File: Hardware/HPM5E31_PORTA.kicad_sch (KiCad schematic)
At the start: 5 parts, among them U1 HPM5E31IGN1

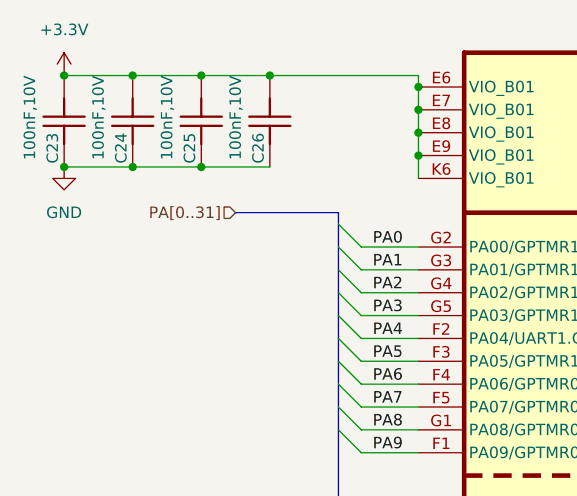
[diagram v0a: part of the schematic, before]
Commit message: 新增ESC IO引出，ESC CTR LED，EUI接口
编码器接口电源输出加保险，SPI加ESD
PY32ADC外部接口加ESD
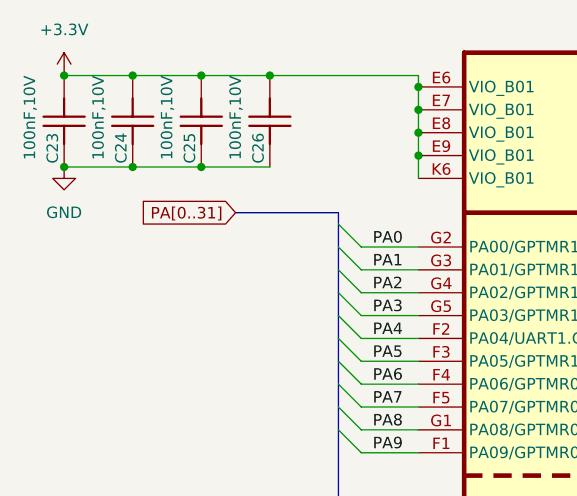
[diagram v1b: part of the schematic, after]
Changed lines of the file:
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@@
 		)
 	)
-	(hierarchical_label "PA[0..31]"
+	(global_label "PA[0..31]"
 		(shape input)
 		(at 99.06 64.77 180)
+		(fields_autoplaced yes)
 		(effects
 			(font
@@
 			(justify right)
 		)
+		(property "Intersheetrefs" "${INTERSHEET_REFS}"
+			(at 87.1847 64.77 0)
+			(effects
+				(font
+					(size 1.27 1.27)
+				)
+				(justify right)
+				(hide yes)
+			)
+		)
 	)

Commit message: 拉线
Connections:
- net +3.3V: now also U1.M1 (DCDC_IN), U1.M2 (DCDC_IN); no longer U1.E6 (VIO_B01), U1.E7 (VIO_B01), U1.E8 (VIO_B01), U1.E9 (VIO_B01), U1.K6 (VIO_B01)
- net PA0: no longer U1.G2 (PA00/GPTMR1.COMP0/UART0.TXD/MCAN0.TXD/PWM0.P0/TRGM.P00/SYSCTL.CLK_OBS0)
- net PA1: no longer U1.G3 (PA01/GPTMR1.CAPT0/UART0.RXD/MCAN0.RXD/PWM0.P1/TRGM.P01/SYSCTL.CLK_OBS2)
- net PA16: no longer U1.L1 (PA16/GPTMR3.COMP0/UART4.TXD/ESC0.P0_RXDV/QEO1.A/SDM0.DAT3/EUI0.CK)
- net PA17: now also U1.H8 (VSSA); no longer U1.L2 (PA17/GPTMR3.CAPT0/UART4.RXD/ESC0.P0_RXD0/QEO1.B/SDM0.CLK3/EUI0.SH)
- net PA18: no longer U1.K1 (PA18/GPTMR3.COMP1/UART4.DE/UART4.RTS/ESC0.P0_RXD1/QEO1.Z/SDM0.DAT2/EUI0.DI)
- net PA19: no longer U1.K2 (PA19/GPTMR3.CAPT1/UART4.CTS/SPI3.CS3/ESC0.P0_RXD2/SDM0.CLK2/EUI0.DO)
- net PA2: no longer U1.G4 (PA02/GPTMR1.COMP1/UART0.DE/UART0.RTS/I2C2.SCL/MCAN0.STBY/PWM0.P2/TRGM.P02/SYSCTL.CLK_OBS1)
- net PA20: no longer U1.J1 (PA20/UART5.CTS/SPI2.SCLK/ESC0.P0_RXD3/SDM0.DAT1)
- net PA21: no longer U1.J2 (PA21/GPTMR3.COMP2/UART5.DE/UART5.RTS/SPI2.CS0/ESC0.P0_RXCK/QEO0.Z/SDM0.CLK1/OWR0.DAT)
- net PA22: no longer U1.H1 (PA22/GPTMR2.CAPT0/UART5.RXD/SPI2.MISO/ETH0.TXER/QEO0.B/SDM0.DAT0/OWR1.DAT)
- net PA23: no longer U1.H2 (PA23/GPTMR2.COMP0/UART5.TXD/SPI2.MOSI/ESC0.P0_RXER/ETH0.RXER/QEO0.A/SDM0.CLK0)
- net PA24: no longer U1.K3 (PA24/GPTMR2.COMP1/UART6.TXD/SPI3.CS2/ESC0.P0_TXCK)
- net PA25: no longer U1.K4 (PA25/GPTMR2.CAPT1/UART6.RXD/SPI3.CS1/ESC0.P0_TXD0/ESC0.CTR0)
- net PA26: no longer U1.J3 (PA26/GPTMR2.COMP2/UART6.DE/UART6.RTS/SPI3.SCLK/ESC0.P0_TXD1/QEI1.H1/EWDG0.RST)
- net PA27: no longer U1.J4 (PA27/UART6.CTS/SPI3.CS0/ESC0.P0_TXD2/QEI1.F)
- net PA28: no longer U1.J5 (PA28/UART7.CTS/SPI3.MISO/ESC0.P0_TXD3/ESC0.CTR1/QEI1.H0)
- net PA29: no longer U1.H3 (PA29/GPTMR3.COMP3/UART7.DE/UART7.RTS/SPI3.MOSI/ESC0.P0_TXEN/QEI1.Z)
- net PA3: no longer U1.G5 (PA03/GPTMR1.CAPT1/UART0.CTS/I2C2.SDA/MCAN1.STBY/PWM0.P3/TRGM.P03/SYSCTL.CLK_OBS3)
- net PA30: no longer U1.H4 (PA30/UART7.RXD/SPI3.DAT2/ESC0.MDIO/ETH0.MDIO/QEI1.A)
- net PA31: no longer U1.H5 (PA31/GPTMR2.COMP3/UART7.TXD/SPI3.DAT3/ESC0.MDC/ETH0.MDC/QEI1.B)
- net PA4: no longer U1.F2 (PA04/UART1.CTS/SPI1.SCLK/MCAN1.RXD/PWM0.P4/TRGM.P04/JTAG.TDO)
- net PA5: no longer U1.F3 (PA05/GPTMR1.COMP2/UART1.DE/UART1.RTS/SPI1.CS0/MCAN1.TXD/PWM0.P5/TRGM.P05/JTAG.TDI)
- net PA6: no longer U1.F4 (PA06/GPTMR0.CAPT0/UART1.RXD/I2C3.SDA/SPI1.MISO/PWM0.P6/TRGM.P06/JTAG.TCK)
- net PA7: no longer U1.F5 (PA07/GPTMR0.COMP0/UART1.TXD/I2C3.SCL/SPI1.MOSI/PWM0.P7/TRGM.P07/JTAG.TMS)
- net PA8: no longer U1.G1 (PA08/GPTMR0.COMP1/UART2.TXD/I2C0.SCL/MCAN2.TXD/PWM1.P0/TRGM.P08/JTAG.TRST)
- net PA9: no longer U1.F1 (PA09/GPTMR0.CAPT1/UART2.RXD/I2C0.SDA/MCAN2.RXD/ESC0.REFCK/PWM1.P1/TRGM.P09)
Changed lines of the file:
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@@
 		(pin "2"
-		)
-		(instances
-			(project "HPM5E31_ECatDualFOC"
-				(path "/a07e9810-3899-4327-ba8f-f24142a7c70e/b9a8d5a3-7d25-4818-87f6-adc719379948/e6555b0c-8db6-46b9-9ffc-fd9d93cb8d54"
-					(reference "C23")
-					(unit 1)
-				)
-			)
 		)
 	)
@@
 		(pin "2"
 		)
-		(instances
-			(project "HPM5E31_ECatDualFOC"
-				(path "/a07e9810-3899-4327-ba8f-f24142a7c70e/b9a8d5a3-7d25-4818-87f6-adc719379948/e6555b0c-8db6-46b9-9ffc-fd9d93cb8d54"
-					(reference "C25")
-					(unit 1)
-				)
-			)
-		)
 	)
 	(symbol
 		(lib_id "HPM5E00_Library:HPM5E31IGN1")
 		(at 124.46 46.99 0)
-		(unit 4)
+		(unit 1)
 		(exclude_from_sim no)
 		(in_bom yes)
@@
 		)
 		(pin "L6"
-		)
-		(instances
-			(project "HPM5E31_ECatDualFOC"
-				(path "/a07e9810-3899-4327-ba8f-f24142a7c70e/b9a8d5a3-7d25-4818-87f6-adc719379948/e6555b0c-8db6-46b9-9ffc-fd9d93cb8d54"
-					(reference "U1")
-					(unit 4)
-				)
-			)
 		)
 	)
@@
 		(pin "2"
 		)
-		(instances
-			(project "HPM5E31_ECatDualFOC"
-				(path "/a07e9810-3899-4327-ba8f-f24142a7c70e/b9a8d5a3-7d25-4818-87f6-adc719379948/e6555b0c-8db6-46b9-9ffc-fd9d93cb8d54"
-					(reference "C26")
-					(unit 1)
-				)
-			)
-		)
 	)
 	(symbol
@@
 		(pin "2"
 		)
-		(instances
-			(project "HPM5E31_ECatDualFOC"
-				(path "/a07e9810-3899-4327-ba8f-f24142a7c70e/b9a8d5a3-7d25-4818-87f6-adc719379948/e6555b0c-8db6-46b9-9ffc-fd9d93cb8d54"
-					(reference "C24")
-					(unit 1)
-				)
-			)
-		)
 	)
 	(symbol
@@
 		(pin "1"
 		)
-		(instances
-			(project "HPM5E31_ECatDualFOC"
-				(path "/a07e9810-3899-4327-ba8f-f24142a7c70e/b9a8d5a3-7d25-4818-87f6-adc719379948/e6555b0c-8db6-46b9-9ffc-fd9d93cb8d54"
-					(reference "#PWR031")
-					(unit 1)
-				)
-			)
-		)
 	)
 	(symbol
@@
 		(pin "1"
 		)
-		(instances
-			(project "HPM5E31_ECatDualFOC"
-				(path "/a07e9810-3899-4327-ba8f-f24142a7c70e/b9a8d5a3-7d25-4818-87f6-adc719379948/e6555b0c-8db6-46b9-9ffc-fd9d93cb8d54"
-					(reference "#PWR032")
-					(unit 1)
-				)
-			)
-		)
 	)

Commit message: 修存档拉线
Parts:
- renumbered C23 to C5, C24 to C6, C25 to C7, C26 to C8, U1 to U3
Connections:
- net +3.3V: now also U3.K6 (VIO_B01); no longer U3.M1 (DCDC_IN), U3.M2 (DCDC_IN)
- net PA0: now also U3.G2 (PA00/GPTMR1.COMP0/UART0.TXD/MCAN0.TXD/PWM0.P0/TRGM.P00/SYSCTL.CLK_OBS0)
- net PA1: now also U3.G3 (PA01/GPTMR1.CAPT0/UART0.RXD/MCAN0.RXD/PWM0.P1/TRGM.P01/SYSCTL.CLK_OBS2)
- net PA16: now also U3.L1 (PA16/GPTMR3.COMP0/UART4.TXD/ESC0.P0_RXDV/QEO1.A/SDM0.DAT3/EUI0.CK)
- net PA17: now also U3.L2 (PA17/GPTMR3.CAPT0/UART4.RXD/ESC0.P0_RXD0/QEO1.B/SDM0.CLK3/EUI0.SH); no longer U3.H8 (VSSA)
- net PA18: now also U3.K1 (PA18/GPTMR3.COMP1/UART4.DE/UART4.RTS/ESC0.P0_RXD1/QEO1.Z/SDM0.DAT2/EUI0.DI)
- net PA19: now also U3.K2 (PA19/GPTMR3.CAPT1/UART4.CTS/SPI3.CS3/ESC0.P0_RXD2/SDM0.CLK2/EUI0.DO)
- net PA2: now also U3.G4 (PA02/GPTMR1.COMP1/UART0.DE/UART0.RTS/I2C2.SCL/MCAN0.STBY/PWM0.P2/TRGM.P02/SYSCTL.CLK_OBS1)
- net PA20: now also U3.J1 (PA20/UART5.CTS/SPI2.SCLK/ESC0.P0_RXD3/SDM0.DAT1)
- net PA21: now also U3.J2 (PA21/GPTMR3.COMP2/UART5.DE/UART5.RTS/SPI2.CS0/ESC0.P0_RXCK/QEO0.Z/SDM0.CLK1/OWR0.DAT)
- net PA22: now also U3.H1 (PA22/GPTMR2.CAPT0/UART5.RXD/SPI2.MISO/ETH0.TXER/QEO0.B/SDM0.DAT0/OWR1.DAT)
- net PA23: now also U3.H2 (PA23/GPTMR2.COMP0/UART5.TXD/SPI2.MOSI/ESC0.P0_RXER/ETH0.RXER/QEO0.A/SDM0.CLK0)
- net PA24: now also U3.K3 (PA24/GPTMR2.COMP1/UART6.TXD/SPI3.CS2/ESC0.P0_TXCK)
- net PA25: now also U3.K4 (PA25/GPTMR2.CAPT1/UART6.RXD/SPI3.CS1/ESC0.P0_TXD0/ESC0.CTR0)
- net PA26: now also U3.J3 (PA26/GPTMR2.COMP2/UART6.DE/UART6.RTS/SPI3.SCLK/ESC0.P0_TXD1/QEI1.H1/EWDG0.RST)
- net PA27: now also U3.J4 (PA27/UART6.CTS/SPI3.CS0/ESC0.P0_TXD2/QEI1.F)
- net PA28: now also U3.J5 (PA28/UART7.CTS/SPI3.MISO/ESC0.P0_TXD3/ESC0.CTR1/QEI1.H0)
- net PA29: now also U3.H3 (PA29/GPTMR3.COMP3/UART7.DE/UART7.RTS/SPI3.MOSI/ESC0.P0_TXEN/QEI1.Z)
- net PA3: now also U3.G5 (PA03/GPTMR1.CAPT1/UART0.CTS/I2C2.SDA/MCAN1.STBY/PWM0.P3/TRGM.P03/SYSCTL.CLK_OBS3)
- net PA30: now also U3.H4 (PA30/UART7.RXD/SPI3.DAT2/ESC0.MDIO/ETH0.MDIO/QEI1.A)
- net PA31: now also U3.H5 (PA31/GPTMR2.COMP3/UART7.TXD/SPI3.DAT3/ESC0.MDC/ETH0.MDC/QEI1.B)
- net PA4: now also U3.F2 (PA04/UART1.CTS/SPI1.SCLK/MCAN1.RXD/PWM0.P4/TRGM.P04/JTAG.TDO)
- net PA5: now also U3.F3 (PA05/GPTMR1.COMP2/UART1.DE/UART1.RTS/SPI1.CS0/MCAN1.TXD/PWM0.P5/TRGM.P05/JTAG.TDI)
- net PA6: now also U3.F4 (PA06/GPTMR0.CAPT0/UART1.RXD/I2C3.SDA/SPI1.MISO/PWM0.P6/TRGM.P06/JTAG.TCK)
- net PA7: now also U3.F5 (PA07/GPTMR0.COMP0/UART1.TXD/I2C3.SCL/SPI1.MOSI/PWM0.P7/TRGM.P07/JTAG.TMS)
- net PA8: now also U3.G1 (PA08/GPTMR0.COMP1/UART2.TXD/I2C0.SCL/MCAN2.TXD/PWM1.P0/TRGM.P08/JTAG.TRST)
- net PA9: now also U3.F1 (PA09/GPTMR0.CAPT1/UART2.RXD/I2C0.SDA/MCAN2.RXD/ESC0.REFCK/PWM1.P1/TRGM.P09)
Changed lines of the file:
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@@
-	)
-	(junction
-		(at 119.38 50.8)
-		(diameter 0)
-		(color 0 0 0 0)
 	)
 	(junction
@@
 	)
 	(junction
-		(at 119.38 55.88)
-		(diameter 0)
-		(color 0 0 0 0)
-	)
-	(junction
-		(at 119.38 53.34)
-		(diameter 0)
-		(color 0 0 0 0)
-	)
-	(junction
 		(at 87.63 49.53)
 		(diameter 0)
@@
 		(color 0 0 0 0)
 	)
-	(junction
-		(at 119.38 58.42)
-		(diameter 0)
-		(color 0 0 0 0)
-	)
 	(bus_entry
 		(at 110.49 66.04)
@@
 	(wire
 		(pts
-			(xy 119.38 60.96) (xy 119.38 58.42)
-		)
-		(stroke
-			(width 0)
-			(type default)
-		)
-	)
-	(wire
-		(pts
 			(xy 113.03 68.58) (xy 119.38 68.58)
 		)
@@
 		)
 	)
-	(wire
-		(pts
-			(xy 119.38 50.8) (xy 119.38 49.53)
-		)
-		(stroke
-			(width 0)
-			(type default)
-		)
-	)
 	(bus
 		(pts
@@
 		)
 	)
-	(wire
-		(pts
-			(xy 119.38 53.34) (xy 119.38 50.8)
-		)
-		(stroke
-			(width 0)
-			(type default)
-		)
-	)
 	(bus
 		(pts
@@
 		)
 	)
-	(wire
-		(pts
-			(xy 119.38 55.88) (xy 119.38 53.34)
-		)
-		(stroke
-			(width 0)
-			(type default)
-		)
-	)
 	(bus
 		(pts
@@
 	(wire
 		(pts
-			(xy 119.38 58.42) (xy 119.38 55.88)
+			(xy 119.38 49.53) (xy 119.38 60.96)
 		)
 		(stroke
@@
 		(dnp no)
 		(fields_autoplaced yes)
-		(property "Reference" "C23"
+		(property "Reference" "C5"
 			(at 78.74 55.88 0)
 			(effects
@@
 		)
 		(pin "2"
+		)
+		(instances
+			(project "HPM5E31_ECatDualFOC"
+				(path "/a07e9810-3899-4327-ba8f-f24142a7c70e/b9a8d5a3-7d25-4818-87f6-adc719379948/e6555b0c-8db6-46b9-9ffc-fd9d93cb8d54"
+					(reference "C5")
+					(unit 1)
+				)
+			)
 		)
 	)
@@
 		(dnp no)
 		(fields_autoplaced yes)
-		(property "Reference" "C25"
+		(property "Reference" "C7"
 			(at 93.98 55.88 0)
 			(effects
@@
 		)
 		(pin "2"
+		)
+		(instances
+			(project "HPM5E31_ECatDualFOC"
+				(path "/a07e9810-3899-4327-ba8f-f24142a7c70e/b9a8d5a3-7d25-4818-87f6-adc719379948/e6555b0c-8db6-46b9-9ffc-fd9d93cb8d54"
+					(reference "C7")
+					(unit 1)
+				)
+			)
 		)
 	)
@@
 		(lib_id "HPM5E00_Library:HPM5E31IGN1")
 		(at 124.46 46.99 0)
-		(unit 1)
+		(unit 4)
 		(exclude_from_sim no)
 		(in_bom yes)
@@
 		(dnp no)
 		(fields_autoplaced yes)
-		(property "Reference" "U1"
+		(property "Reference" "U3"
 			(at 233.68 93.9799 0)
 			(effects
@@
 		)
 		(pin "L6"
+		)
+		(instances
+			(project "HPM5E31_ECatDualFOC"
+				(path "/a07e9810-3899-4327-ba8f-f24142a7c70e/b9a8d5a3-7d25-4818-87f6-adc719379948/e6555b0c-8db6-46b9-9ffc-fd9d93cb8d54"
+					(reference "U3")
+					(unit 4)
+				)
+			)
 		)
 	)
@@
 		(dnp no)
 		(fields_autoplaced yes)
-		(property "Reference" "C26"
+		(property "Reference" "C8"
 			(at 101.6 55.88 0)
 			(effects
@@
 		)
 		(pin "2"
+		)
+		(instances
+			(project "HPM5E31_ECatDualFOC"
+				(path "/a07e9810-3899-4327-ba8f-f24142a7c70e/b9a8d5a3-7d25-4818-87f6-adc719379948/e6555b0c-8db6-46b9-9ffc-fd9d93cb8d54"
+					(reference "C8")
+					(unit 1)
+				)
+			)
 		)
 	)
@@
 		(dnp no)
 		(fields_autoplaced yes)
-		(property "Reference" "C24"
+		(property "Reference" "C6"
 			(at 86.36 55.88 0)
 			(effects
@@
 		)
 		(pin "2"
+		)
+		(instances
+			(project "HPM5E31_ECatDualFOC"
+				(path "/a07e9810-3899-4327-ba8f-f24142a7c70e/b9a8d5a3-7d25-4818-87f6-adc719379948/e6555b0c-8db6-46b9-9ffc-fd9d93cb8d54"
+					(reference "C6")
+					(unit 1)
+				)
+			)
 		)
 	)
@@
 		(dnp no)
 		(fields_autoplaced yes)
-		(property "Reference" "#PWR031"
+		(property "Reference" "#PWR046"
 			(at 80.01 53.34 0)
 			(effects
@@
 		)
 		(pin "1"
+		)
+		(instances
+			(project "HPM5E31_ECatDualFOC"
+				(path "/a07e9810-3899-4327-ba8f-f24142a7c70e/b9a8d5a3-7d25-4818-87f6-adc719379948/e6555b0c-8db6-46b9-9ffc-fd9d93cb8d54"
+					(reference "#PWR046")
+					(unit 1)
+				)
+			)
 		)
 	)
@@
 		(dnp no)
 		(fields_autoplaced yes)
-		(property "Reference" "#PWR032"
+		(property "Reference" "#PWR047"
 			(at 80.01 66.04 0)
 			(effects
@@
 		(pin "1"
 		)
-	)
+		(instances
+			(project "HPM5E31_ECatDualFOC"
+				(path "/a07e9810-3899-4327-ba8f-f24142a7c70e/b9a8d5a3-7d25-4818-87f6-adc719379948/e6555b0c-8db6-46b9-9ffc-fd9d93cb8d54"
+					(reference "#PWR047")
+					(unit 1)
+				)
+			)
+		)
+	)

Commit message: 拉线
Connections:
- net +3.3V: now also U3.E6 (VIO_B01), U3.E7 (VIO_B01), U3.E8 (VIO_B01), U3.E9 (VIO_B01)
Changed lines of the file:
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@@
 	(paper "A4")
 	(junction
+		(at 119.38 58.42)
+		(diameter 0)
+		(color 0 0 0 0)
+	)
+	(junction
+		(at 119.38 53.34)
+		(diameter 0)
+		(color 0 0 0 0)
+	)
+	(junction
+		(at 119.38 50.8)
+		(diameter 0)
+		(color 0 0 0 0)
+	)
+	(junction
 		(at 80.01 59.69)
 		(diameter 0)
@@
 	)
 	(junction
+		(at 119.38 55.88)
+		(diameter 0)
+		(color 0 0 0 0)
+	)
+	(junction
 		(at 95.25 59.69)
 		(diameter 0)
@@
 	(wire
 		(pts
+			(xy 119.38 53.34) (xy 119.38 55.88)
+		)
+		(stroke
+			(width 0)
+			(type default)
+		)
+	)
+	(wire
+		(pts
 			(xy 113.03 81.28) (xy 119.38 81.28)
 		)
@@
 		)
 	)
+	(wire
+		(pts
+			(xy 119.38 50.8) (xy 119.38 53.34)
+		)
+		(stroke
+			(width 0)
+			(type default)
+		)
+	)
 	(bus
 		(pts
@@
 	(wire
 		(pts
+			(xy 119.38 55.88) (xy 119.38 58.42)
+		)
+		(stroke
+			(width 0)
+			(type default)
+		)
+	)
+	(wire
+		(pts
 			(xy 113.03 123.19) (xy 119.38 123.19)
 		)
@@
 	(wire
 		(pts
-			(xy 119.38 49.53) (xy 119.38 60.96)
+			(xy 119.38 49.53) (xy 119.38 50.8)
 		)
 		(stroke
@@
 		)
 		(stroke
+			(width 0)
+			(type default)
+		)
+	)
+	(wire
+		(pts
+			(xy 119.38 58.42) (xy 119.38 60.96)
+		)
+		(stroke
